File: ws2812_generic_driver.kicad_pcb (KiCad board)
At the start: 2 copper layers, 18 x 12.5 mm, 15 parts, among them J1 Conn_01x01, J2 Conn_01x01, J3 Conn_ARM_JTAG_SWD_10, J4 Conn_01x01, J5 Conn_01x01, J6 Conn_01x01, J7 Conn_01x01, U1 ATSAMD21E15L-A, U2 TC2014-3.3VxCTTR

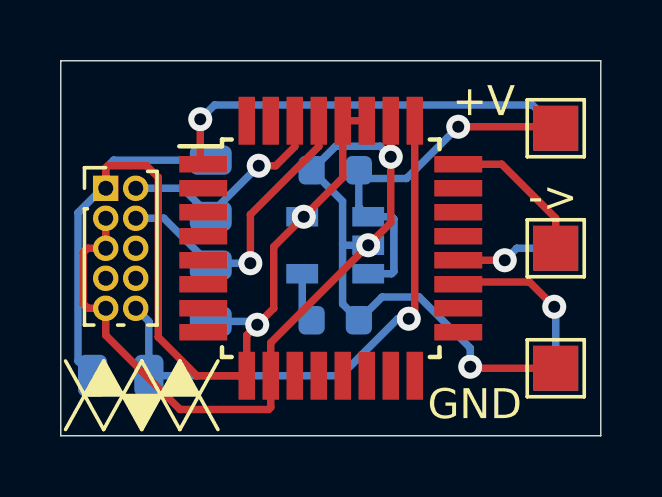
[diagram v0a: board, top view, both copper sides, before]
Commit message: Add attiny10 hardware spi->ws2812 support
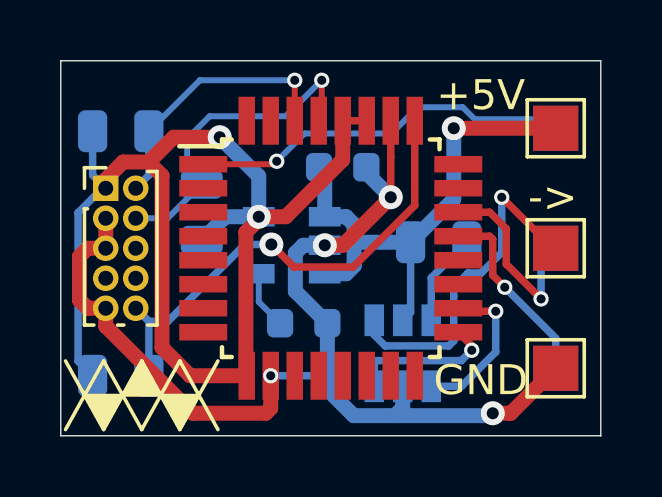
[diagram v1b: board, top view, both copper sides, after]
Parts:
- added R4: 10kR, Resistor_SMD:R_0805_2012Metric, B.Cu at (148.1, 103.8)
- added U3: ATtiny10-TS, Package_TO_SOT_SMD:SOT-23-6, B.Cu at (146.9, 107.5)
- moved R3 3.55 mm to (137.5, 100.1), turned to 0 degrees
- moved R2 2.72 mm to (140.2, 102.8)
- moved U2 1.45 mm to (143.2, 103.9)
- moved C1 1.05 mm to (143.6, 106.5)
- moved C2 0.27 mm to (144.9, 101.3), turned to 0 degrees
- turned REF** to 0 degrees
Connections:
- net +V renamed +5V
- U1 pad 17: (no net) -> MOSI
- U1 pad 18: (no net) -> SCK
- U1 pad 19: D2 -> (no net)
- U1 pad 20: D1 -> (no net)
- U1 pad 21: (no net) -> D2
- U1 pad 22: (no net) -> D1
- U1 pad 24: DOUT -> (no net)
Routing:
- net DOUT: track 5.00 -> 11.6 mm, vias 0 -> 1
- net SCK: track 0.00 -> 5.27 mm, vias 0 -> 1
- net +5V: track 12.6 -> 17.7 mm
- net +3.3V: track 34.8 -> 39.8 mm
- net MOSI: track 0.00 -> 4.99 mm, vias 0 -> 1
- net GND: track 40.9 -> 37.3 mm, vias 3 -> 4
- net D1: track 3.42 -> 6.54 mm
- net Net-(R4-Pad2): track 0.00 -> 3.09 mm
- net RESET: track 18.6 -> 16.3 mm
- net SWDIO: track 7.57 -> 9.00 mm
- net A1: track 13.9 -> 12.8 mm
- net SWCLK: track 10.2 -> 11.1 mm
- net D2: track 5.64 -> 6.36 mm
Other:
- board text added: "+5V"
- board text added: "v0.0.0 11/13/20"
- board text removed: "+V"
- board text removed: "v0.0.0 11/11/20"
